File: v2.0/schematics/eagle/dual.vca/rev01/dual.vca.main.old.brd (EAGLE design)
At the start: 86 x 99 mm, 92 parts, among them IC1 TL082P, IC2 TL084P, IC3 LM324N, T1 BC547, T2 BC547, T3 BC547, T4 BC547, T5 BC547, T6 BC547

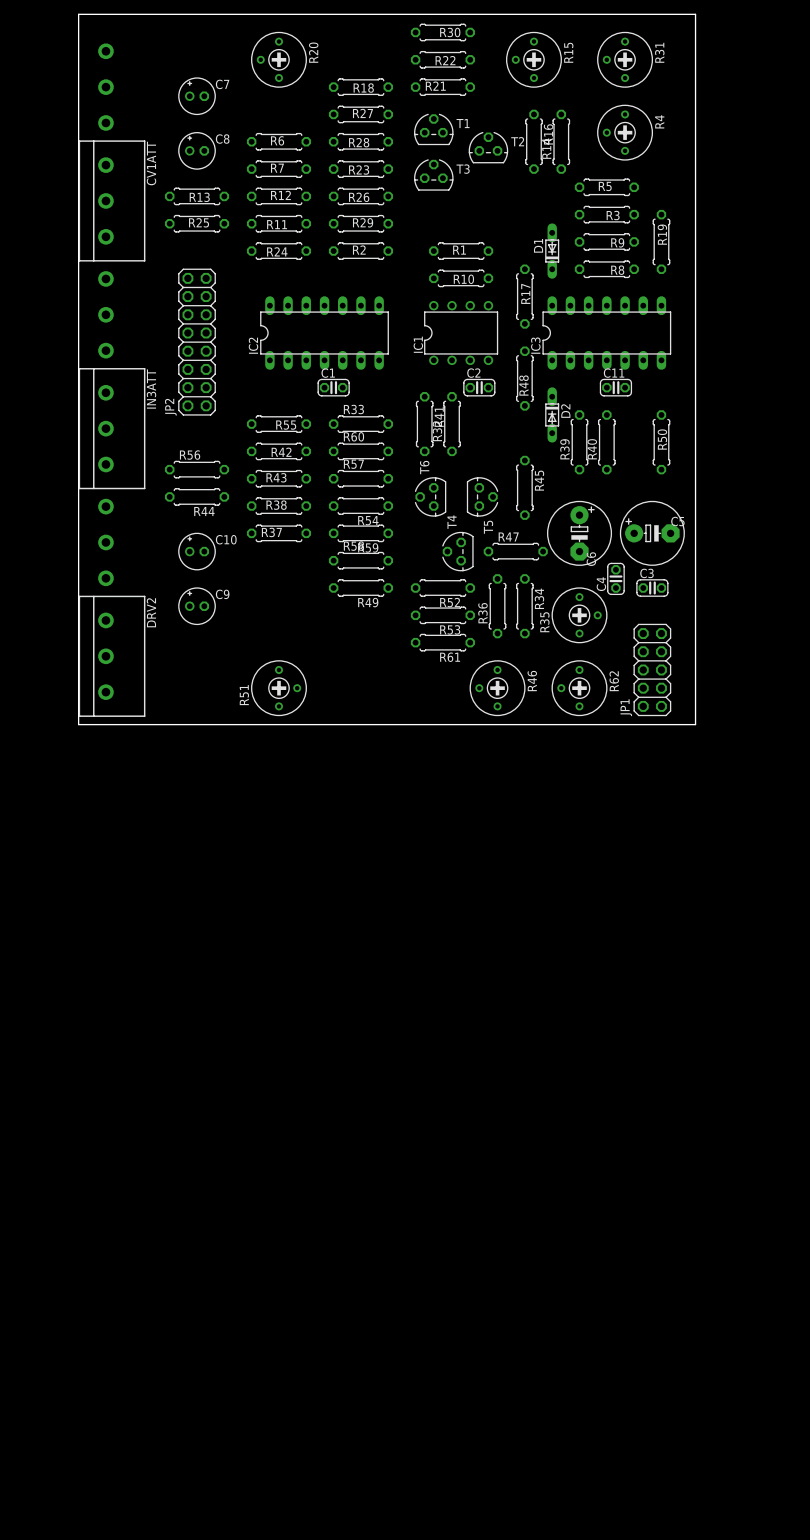
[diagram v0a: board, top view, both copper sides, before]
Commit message: Iniital board layout for main dual.vca
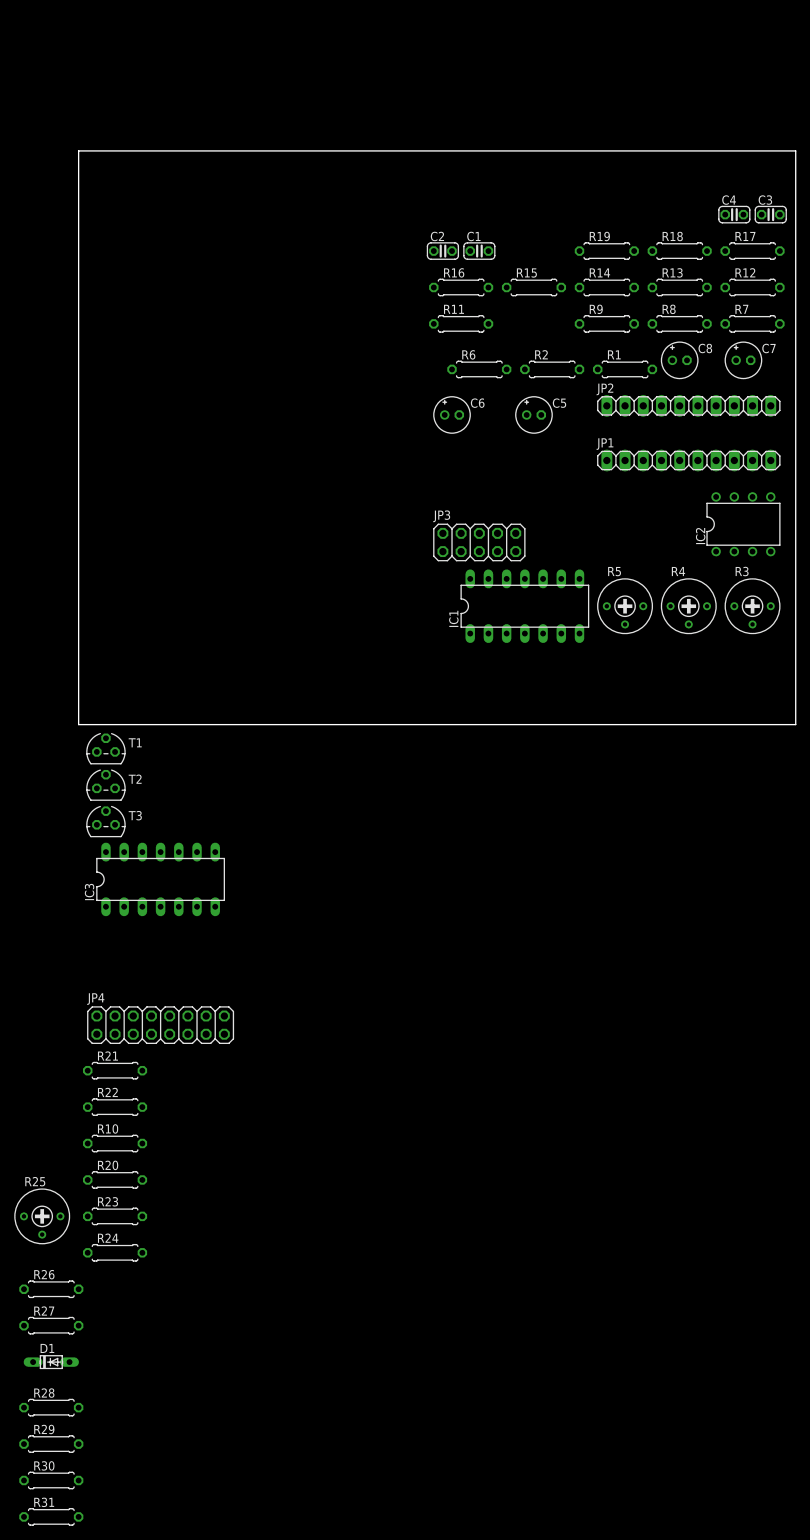
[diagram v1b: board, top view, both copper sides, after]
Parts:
- removed C10: 2.2uF, _common:E2-5
- removed C11: 0.1uF, _common:C025-024X044
- removed C9: 2.2 uF, _common:E2-5
- removed CV1ATT, CV3ATT: 250K LIN, _common:3RP/1610N
- removed D2: 1N4148, _common:DO34-5
- removed DRV1, DRV2: 10K LIN, _common:3RP/1610N
- removed IN1ATT, IN3ATT: 250K LOG, _common:3RP/1610N
- removed R32, R33, R34, R36, R37, R38, R41, R42, R43, R59, R60: 100K, _common:0207/7
- removed R35: 250K, rcl:RTRIM3339P
- removed R39, R40: 1M, _common:0207/7
- removed R44, R56: 1K, _common:0207/7
- removed R45: 22K, _common:0207/7
- removed R46, R62: 100K, rcl:RTRIM3339P
- removed R47: 5K, _common:0207/7
- removed R48, R50: 3.3K, _common:0207/7
- removed R49, R53, R54: 15K, _common:0207/7
- removed R51: 1K, rcl:RTRIM3339P
- removed R52: 33K, _common:0207/7
- removed R55: 1.2K, _common:0207/7
- removed R57, R58: 10K, _common:0207/7
- removed R61: 470K, _common:0207/7
- removed T4, T5, T6: BC547, transistor:TO92
- added JP3: (no value), pinhead:2X05
- added JP4: (no value), pinhead:2X08
- C5: value 100uF -> 2.2 uF; device _common:E5-8,5 -> _common:E2-5
- C6: value 100uF -> 2.2uF; device _common:E5-8,5 -> _common:E2-5
- C7: value 2.2 uF -> 100uF
- C8: value 2.2uF -> 100uF
- IC1: value TL082P -> TL084P; device linear:DIL08 -> linear:DIL14
- IC2: value TL084P -> TL082P; device linear:DIL14 -> linear:DIL08
- JP1: value (none) -> VCA1-2; device pinhead:2X05 -> pinhead:1X10
- JP2: value (none) -> VCA3-4; device pinhead:2X08 -> pinhead:1X10
- R1, R2: value 100K -> 15K
- R11, R12: value 100K -> 10K
- R13: value 1K -> 100K
- R14: value 22K -> 470K
- R15: device rcl:RTRIM3339P -> _common:0207/7
- R16: value 5K -> 100K
- R17: value 3.3K -> 100K
- R18: value 15K -> 1K
- R19: value 3.3K -> 15K
- R20: value 1K -> 100K; device rcl:RTRIM3339P -> _common:0207/7
- R21: value 33K -> 100K
- R22: value 15K -> 100K
- R23: value 15K -> 1M
- R24: value 1.2K -> 1M
- R25: value 1K -> 250K; device _common:0207/7 -> rcl:RTRIM3339P
- R26, R27: value 10K -> 100K
- R28, R29: value 100K -> 3.3K
- R3: value 100K -> 1K; device _common:0207/7 -> rcl:RTRIM3339P
- R30: value 470K -> 1.2K
- R31: value 100K -> 1K; device rcl:RTRIM3339P -> _common:0207/7
- R4: value 250K -> 100K
- R5: device _common:0207/7 -> rcl:RTRIM3339P
- R6: value 100K -> 33K
- R7: value 100K -> 5K
- R8: value 1M -> 22K
- R9: value 1M -> 100K
- moved R31 218.4 mm to (-3.81, -110.5), turned to 0 degrees
- moved R30 209.2 mm to (-3.81, -105.4), turned to 0 degrees
- moved R28 181.7 mm to (-3.81, -95.2), turned to 0 degrees
- moved R29 175.6 mm to (-3.81, -100.3)
- moved R27 174.3 mm to (-3.81, -83.8)
- moved D1 170.0 mm to (-3.81, -88.9), turned to 0 degrees
- moved R26 158.4 mm to (-3.81, -78.7), turned to 0 degrees
- moved R20 157.9 mm to (5.08, -63.5), turned to 0 degrees
- moved R22 153.0 mm to (5.08, -53.3), turned to 0 degrees
- moved R23 150.0 mm to (5.08, -68.6), turned to 0 degrees
- moved R21 144.6 mm to (5.08, -48.3)
- moved R24 141.6 mm to (5.08, -73.7), turned to 0 degrees
- moved R25 140.1 mm to (-5.08, -68.6)
- moved R10 129.9 mm to (5.08, -58.4), turned to 0 degrees
- moved T2 103.7 mm to (3.81, -8.89)
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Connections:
- removed net N$26: DRV2.2, DRV2.3, R44.2
- removed net N$27: C7.+, IN1ATT.2
- removed net N$28: IC2.2, R37.2, R38.2, R42.1
- removed net N$29: CV1ATT.2, R1.1
- removed net N$30: IC2.1, R42.2, R43.1
- removed net N$31: R49.1, R58.1, T4.3
- removed net N$32: R49.2, R51.1
- removed net N$33: R51.3, R54.2
- removed net N$34: R54.1, R57.1, T6.3
- removed net N$35: R52.2, T4.1, T6.1
- removed net N$36: IC2.6, R57.2, R60.1
- removed net N$37: IC2.5, R58.2, R59.2, R61.2
- removed net N$38: R61.1, R62.2
- removed net N$39: R52.1, R53.2, T5.1
- removed net N$40: R45.2, R47.2, T5.2
- removed net N$41: R46.2, R47.1
- removed net N$42: IC1.1, R41.2, R45.1
- removed net N$43: IC1.2, IC3.2, R32.2, R33.2, R39.2, R41.1
- removed net N$44: C9.-, R37.1
- removed net N$45: C10.-, R38.1
- removed net N$46: IC3.3, R35.2, R40.2
- removed net N$47: R34.1, R35.3
- removed net N$48: R35.1, R36.2
- removed net N$49: D2.C, IC3.1
- removed net N$50: D2.A, R48.1
- removed net N$51: IC3.6, R48.2, R50.1
- removed net N$52: IC3.7, R50.2, R55.1
- removed net N$53: DRV2.1, R43.2, T4.2
- removed net N$54: DRV1.2, DRV1.3, R13.2
- removed net N$55: C9.+, IN3ATT.2
- removed net N$56: CV3ATT.2, R32.1
- new net CVATT1B: JP4.9, R22.1
- new net CVATT2A: JP4.6
- new net CVATT2B: JP4.8
- new net DRV1A: JP4.11
- new net DRV1B: JP4.13
- new net DRV2A: JP4.10
- new net DRV2B: JP4.12
- new net DRV2C: JP4.14
- new net DVV1C: JP4.15
- new net INATT1B: C5.+, JP4.5
- new net INATT2B: JP4.4
- net +12V: now also C4.1, C7.+, IC1.4, IC2.8, JP3.10, JP3.9, R26.2, R4.3, R5.3; no longer C11.1, C2.1, C5.+, IC1.8, IC2.4, JP1.10, JP1.9, R15.3, R20.2, R31.3, R34.2, R46.3, R51.2, R62.3
- net -12V: now also C3.2, C8.-, IC1.11, IC2.4, JP3.1, JP3.2, R19.1, R27.1, R4.1; no longer C1.2, C11.2, C6.-, IC1.4, IC2.11, JP1.1, JP1.2, R15.1, R22.1, R31.1, R36.1, R46.1, R53.1, R62.1
- net 0V: now also C1.2, C2.1, C7.-, C8.+, JP1.1, JP1.10, JP1.2, JP1.9, JP2.10, JP2.9, JP3.3, JP3.4, JP3.5, JP3.6, JP3.7, JP3.8, JP4.1, JP4.16, R18.1, R23.1, R24.1, R31.1, T2.2, T3.3; no longer C3.2, C4.1, C5.-, C6.+, CV1ATT.1, CV3ATT.1, IC1.5, IC2.12, IC3.10, IN1ATT.1, IN3ATT.1, JP1.3, JP1.4, JP1.5, JP1.6, JP1.7, JP1.8, JP2.15, JP2.16, R25.1, R28.1, R39.1, R40.1, R44.1, R56.1, R59.1, R8.1, R9.1, T2.3, T3.2, T5.3, T6.2
- net CV1: now also JP1.5, JP4.7; no longer CV1ATT.3, JP2.7
- net CV2: now also JP1.6, R21.1; no longer JP2.9, R2.1
- net CV3: now also JP2.5; no longer CV3ATT.3, JP2.8
- net CV4: now also JP2.6; no longer JP2.10, R33.1
- net IN1: now also JP1.3, JP4.3; no longer IN1ATT.3, JP2.3
- net IN2: now also C6.+, JP1.7; no longer C8.+, JP2.11
- net IN3: now also JP2.3, JP4.2; no longer IN3ATT.3, JP2.4
- net IN4: now also JP2.7; no longer C10.+, JP2.12
- net N$1: now also IC1.2, R10.2, R16.1, R20.2; no longer IC2.13, R11.1, R6.2, R7.2
- net N$10: now also R14.1, R5.2; no longer R30.1, R31.2
- net N$11: now also C5.-, R10.1; no longer C7.-, R6.1
- net N$12: now also IC1.5, R12.2, R13.2, R14.2; no longer IC2.10, R27.2, R28.2, R30.2
- net N$13: now also R19.2, R6.1, T3.1; no longer R21.1, R22.2, T2.1
- net N$14: now also C6.-, R20.1; no longer C8.-, R7.1
- net N$15: now also R7.2, R8.2, T3.2; no longer R14.2, R16.2, T2.2
- net N$16: now also R4.2, R7.1; no longer R15.2, R16.1
- net N$17: now also IC2.1, R8.1, R9.2; no longer IC1.7, R10.2, R14.1
- net N$18: now also IC3.3, R24.2, R25.2; no longer IC3.12, R4.2, R9.2
- net N$19: now also IC2.2, IC3.2, R21.2, R22.2, R23.2, R9.1; no longer IC1.6, IC3.13, R1.2, R10.1, R2.2, R8.2
- net N$2: now also IC1.6, R11.2, R15.1; no longer IC2.9, R26.2, R29.1
- net N$20: now also R25.3, R26.1; no longer R3.1, R4.3
- net N$21: now also R25.1, R27.2; no longer R4.1, R5.2
- net N$22: now also IC3.1; no longer IC3.14
- net N$23: now also R28.1; no longer R17.1
- net N$24: now also IC3.6, R28.2, R29.1; no longer IC3.9, R17.2, R19.1
- net N$25: now also IC3.7, R29.2, R30.1; no longer IC3.8, R19.2, R24.1
- net N$3: now also IC1.1, R16.2, R17.1; no longer IC2.14, R11.2, R12.1
- net N$4: now also R17.2, R18.2; no longer DRV1.1, R12.2
- net N$5: now also R1.1, R12.1; no longer R18.1, R27.1
- net N$6: now also R1.2, R3.1; no longer R18.2, R20.1
- net N$7: now also R2.2, R3.3; no longer R20.3, R23.2
- net N$8: now also R11.1, R2.1, T2.3; no longer R23.1, R26.1, T3.3
- net N$9: now also R6.2, T2.1; no longer R21.2, T3.1
- net OUT1: now also IC1.7, JP1.4, R15.2; no longer IC2.8, JP2.5, R29.2
- net OUT2: now also JP1.8, R30.2, R31.2; no longer JP2.13, R24.2, R25.2
- net OUT3: now also JP2.4; no longer IC2.7, JP2.6, R60.2
- net OUT4: now also JP2.8; no longer JP2.14, R55.2, R56.2
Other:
- board size 86 x 99 mm -> 100 x 80 mm
